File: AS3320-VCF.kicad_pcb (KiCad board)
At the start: 2 copper layers, 71.2 x 131.1 mm, 48 parts, among them J1 SIGNAL_INPUT, J2 RESONANCE_CTRL_INPUT, J3 FREQ_CTRL_INPUT, J4 SIGNAL_OUTPUT, J5 -----, U1 AS3320

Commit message: Refactor
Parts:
- removed TP1: RES_CTRL, Seattle_Synths:TestPoint_Pad_4.0x4.0mm
- removed TP2: +12V, Seattle_Synths:TestPoint_Pad_4.0x4.0mm
- removed TP3: -12V, Seattle_Synths:TestPoint_Pad_4.0x4.0mm
- removed TP4: GND, Seattle_Synths:TestPoint_Pad_4.0x4.0mm
- removed TP5: FREQ_CTRL, Seattle_Synths:TestPoint_Pad_4.0x4.0mm
- removed TP6: INPUT, Seattle_Synths:TestPoint_Pad_4.0x4.0mm
- removed TP7: OUTPUT, Seattle_Synths:TestPoint_Pad_4.0x4.0mm
- added C10: 100nF, Seattle_Synths:C_0603_1608Metric, F.Cu at (147.8, 76.5)
- added C11: 470nF, Seattle_Synths:C_0603_1608Metric, F.Cu at (147.8, 83.2)
- added C12: 220pF, Seattle_Synths:C_0603_1608Metric, F.Cu at (92.2, 30.0)
- added C8: 470nF, Seattle_Synths:C_0603_1608Metric, F.Cu at (141.8, 83.2)
- added C9: 22pF, Seattle_Synths:C_0603_1608Metric, F.Cu at (140.2, 46.5)
- added J6: CV2_INPUT, Seattle_Synths:Jack_3.5mm_QingPu_WQP-PJ398SM_Vertical_CircularHoles, F.Cu at (18.8, 78.0)
- added J7: EURO_PWR_2x5, Seattle_Synths:3M_2510-6002UB, F.Cu at (117.0, 87.8)
- added J8: AUDIO_OUTPUT, Seattle_Synths:Jack_3.5mm_QingPu_WQP-PJ398SM_Vertical_CircularHoles, F.Cu at (158.2, 34.5)
- added R22: 91K, Seattle_Synths:R_0603_1608Metric, F.Cu at (84.8, 48.8)
- added R23: 91K, Seattle_Synths:R_0603_1608Metric, F.Cu at (84.8, 51.8)
- added R24: 100K, Seattle_Synths:R_0603_1608Metric, F.Cu at (84.8, 54.8)
- added R25: 240K, Seattle_Synths:R_0603_1608Metric, F.Cu at (84.8, 57.8)
- added R26: 240K, Seattle_Synths:R_0603_1608Metric, F.Cu at (84.8, 60.8)
- added R27: 51K, Seattle_Synths:R_0603_1608Metric, F.Cu at (93.8, 55.5)
- added R28: 1K, Seattle_Synths:R_0603_1608Metric, F.Cu at (105.0, 69.0)
- added R29: 1K, Seattle_Synths:R_0603_1608Metric, F.Cu at (124.5, 20.2)
- added R30: 100K, Seattle_Synths:R_0603_1608Metric, F.Cu at (128.2, 36.0)
- added R31: 180K, Seattle_Synths:R_0603_1608Metric, F.Cu at (130.5, 40.5)
- added R32: 300K, Seattle_Synths:R_0603_1608Metric, F.Cu at (140.2, 40.5)
- added R33: 1K, Seattle_Synths:R_0603_1608Metric, F.Cu at (149.2, 34.5)
- added RV3: 100K lin, Seattle_Synths:Potentiometer_Alpha_RD901F-40-00D_Single_Vertical, F.Cu at (29.2, 94.5)
- added RV4: 100K lin, Seattle_Synths:Potentiometer_Alpha_RD901F-40-00D_Single_Vertical, F.Cu at (29.2, 107.2)
- added RV5: 100K, Seattle_Synths:Potentiometer_Alpha_RD901F-40-00D_Single_Vertical, F.Cu at (36.0, 30.8)
- added RV6: 100K, Seattle_Synths:Potentiometer_Alpha_RD901F-40-00D_Single_Vertical, F.Cu at (36.0, 39.8)
- added RV7: 20K, Seattle_Synths:TRIM_3266W-1-102LF, F.Cu at (48.8, 64.5)
- added RV8: 1K5, Seattle_Synths:TRIM_3266W-1-102LF, F.Cu at (105.0, 63.0)
- added RV9: 100K, Seattle_Synths:TRIM_3266W-1-102LF, F.Cu at (130.5, 46.5)
- added U2: AS3320, Seattle_Synths:DIP-18_W7.62mm_Socket, F.Cu at (105.0, 47.2)
- added U3: TL082, Seattle_Synths:DIP-8_W7.62mm_Socket, F.Cu at (139.5, 34.5)
- C1: value 300pF -> 22pF; footprint Seattle_Synths:C_Disc_D7.5mm_W2.5mm_P5.00mm -> Seattle_Synths:C_0603_1608Metric
- C2: value 300pF -> 1µF; footprint Seattle_Synths:C_Disc_D7.5mm_W2.5mm_P5.00mm -> Seattle_Synths:CP_Radial_D5.0mm_P2.50mm
- C3, C4: value 300pF -> 220pF; footprint Seattle_Synths:C_Disc_D7.5mm_W2.5mm_P5.00mm -> Seattle_Synths:C_0603_1608Metric
- C5: value 1µF -> 220pF; footprint Seattle_Synths:CP_Radial_D5.0mm_P2.50mm -> Seattle_Synths:C_0603_1608Metric
- C6: value 10uF -> 1µF
- C7: value 10uF -> 100nF; footprint Seattle_Synths:CP_Radial_D5.0mm_P2.50mm -> Seattle_Synths:C_0603_1608Metric
- D1: footprint Seattle_Synths:LED_D5.0mm -> Seattle_Synths:D_0603_1608Metric; moved to F.Cu
- J1: value SIGNAL_INPUT -> AUDIO3_INPUT; moved to F.Cu
- J2: value RESONANCE_CTRL_INPUT -> AUDIO2_INPUT; moved to F.Cu
- J3: value FREQ_CTRL_INPUT -> AUDIO1_INPUT; moved to F.Cu
- J4: value SIGNAL_OUTPUT -> RES_INPUT; moved to F.Cu
- J5: value ----- -> 1V/OCT_INPUT; footprint Seattle_Synths:PinHeader_2x05_P2.54mm_Vertical -> Seattle_Synths:Jack_3.5mm_QingPu_WQP-PJ398SM_Vertical_CircularHoles
- R1: value 330R -> 51K; footprint Seattle_Synths:R_Axial_DIN0207_L6.3mm_D2.5mm_P10.16mm_Horizontal -> Seattle_Synths:R_0603_1608Metric
- R10, R19: value 1K8 -> 100K; footprint Seattle_Synths:R_Axial_DIN0207_L6.3mm_D2.5mm_P10.16mm_Horizontal -> Seattle_Synths:R_0603_1608Metric
- R11, R9: footprint Seattle_Synths:R_Axial_DIN0207_L6.3mm_D2.5mm_P10.16mm_Horizontal -> Seattle_Synths:R_0603_1608Metric
- R12: value 100K -> 15K; footprint Seattle_Synths:R_Axial_DIN0207_L6.3mm_D2.5mm_P10.16mm_Horizontal -> Seattle_Synths:R_0603_1608Metric
- R13: value 91K -> 36K; footprint Seattle_Synths:R_Axial_DIN0207_L6.3mm_D2.5mm_P10.16mm_Horizontal -> Seattle_Synths:R_0603_1608Metric
- R14: value 100K -> 56K; footprint Seattle_Synths:R_Axial_DIN0207_L6.3mm_D2.5mm_P10.16mm_Horizontal -> Seattle_Synths:R_0603_1608Metric
- R15: value 91K -> 1K; footprint Seattle_Synths:R_Axial_DIN0207_L6.3mm_D2.5mm_P10.16mm_Horizontal -> Seattle_Synths:R_0603_1608Metric
- R16, R18: value 100K -> 91K; footprint Seattle_Synths:R_Axial_DIN0207_L6.3mm_D2.5mm_P10.16mm_Horizontal -> Seattle_Synths:R_0603_1608Metric
- R17: value 91K -> 100K; footprint Seattle_Synths:R_Axial_DIN0207_L6.3mm_D2.5mm_P10.16mm_Horizontal -> Seattle_Synths:R_0603_1608Metric
- R2: value 72K -> 100K; footprint Seattle_Synths:R_Axial_DIN0207_L6.3mm_D2.5mm_P10.16mm_Horizontal -> Seattle_Synths:R_0603_1608Metric
- R20: value 51K -> 240K; footprint Seattle_Synths:R_Axial_DIN0207_L6.3mm_D2.5mm_P10.16mm_Horizontal -> Seattle_Synths:R_0603_1608Metric
- R21: value 330R -> 100K; footprint Seattle_Synths:R_Axial_DIN0207_L6.3mm_D2.5mm_P10.16mm_Horizontal -> Seattle_Synths:R_0603_1608Metric
- R3: value 50K -> 180K; footprint Seattle_Synths:R_Axial_DIN0207_L6.3mm_D2.5mm_P10.16mm_Horizontal -> Seattle_Synths:R_0603_1608Metric
- R4, R5: value 220K -> 100K; footprint Seattle_Synths:R_Axial_DIN0207_L6.3mm_D2.5mm_P10.16mm_Horizontal -> Seattle_Synths:R_0603_1608Metric
- R6: value 220K -> 150K; footprint Seattle_Synths:R_Axial_DIN0207_L6.3mm_D2.5mm_P10.16mm_Horizontal -> Seattle_Synths:R_0603_1608Metric
- R7: value 50K -> 1M5; footprint Seattle_Synths:R_Axial_DIN0207_L6.3mm_D2.5mm_P10.16mm_Horizontal -> Seattle_Synths:R_0603_1608Metric
- R8: value 100K -> 300K; footprint Seattle_Synths:R_Axial_DIN0207_L6.3mm_D2.5mm_P10.16mm_Horizontal -> Seattle_Synths:R_0603_1608Metric
- RV1: moved to F.Cu
- RV2: value 100K -> 100K lin; moved to F.Cu
- U1: value AS3320 -> TL082; footprint Seattle_Synths:DIP-18_W7.62mm_Socket -> Seattle_Synths:DIP-8_W7.62mm_Socket
- moved C1 164.0 mm to (52.5, 18.8)
- moved J1 156.3 mm to (18.8, 18.8), turned to 0 degrees
- moved J5 147.5 mm to (18.8, 67.5), turned to 0 degrees
- moved J3 139.2 mm to (18.8, 36.8), turned to 0 degrees
- moved C3 131.9 mm to (89.2, 27.0)
- moved C2 130.7 mm to (71.2, 30.8)
- moved J2 127.2 mm to (18.8, 27.8), turned to 0 degrees
- moved J4 125.9 mm to (18.8, 48.8), turned to 0 degrees
- moved RV1 116.7 mm to (27.8, 51.0), turned to 0 degrees
- moved RV2 116.1 mm to (29.2, 80.2), turned to 0 degrees
- moved R11 116.1 mm to (42.8, 64.5)
- moved R12 113.4 mm to (48.0, 37.5)
- moved R13 113.3 mm to (52.5, 30.8)
- moved R8 110.9 mm to (42.0, 18.8)
- moved R21 110.0 mm to (84.8, 45.8)
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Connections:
- C1 pad 1: GND -> Net-(C1-Pad1)
- C2 pad 2: GND -> Net-(C1-Pad2)
- C3 pad 1: GND -> Net-(C3-Pad1)
- C3 pad 2: Net-(C3-Pad2) -> GND
- C4 pad 1: Net-(C4-Pad1) -> GND
- C4 pad 2: GND -> Net-(C4-Pad2)
- C5 pad 1: /OUT4 -> Net-(C5-Pad1)
- C5 pad 2: /SIGNAL_OUTPUT -> GND
- C6 pad 1: -12V -> /OUT4
- C6 pad 2: GND -> Net-(C6-Pad2)
- C7 pad 2: +12V -> -12V
- J1 pad T: /SIGNAL_INPUT -> Net-(J1-PadT)
- J2 pad T: /RESONANCE_CTRL_INPUT -> Net-(J2-PadT)
- J3 pad T: /FREQ_CTRL_INPUT -> Net-(J3-PadT)
- J4 pad T: /SIGNAL_OUTPUT -> Net-(J4-PadT)
- J4 pad TN: (no net) -> Net-(J4-PadTN)
- R1 pad 1: -12V -> Net-(J4-PadTN)
- R1 pad 2: Net-(R1-Pad2) -> +12V
- R10 pad 1: GND -> Net-(C1-Pad1)
- R11 pad 2: /SIGNAL_INPUT -> Net-(R11-Pad2)
- R12 pad 1: Net-(R11-Pad1) -> Net-(R12-Pad1)
- R12 pad 2: /OUT1 -> GND
- R13 pad 1: Net-(R13-Pad1) -> Net-(C1-Pad2)
- R13 pad 2: /OUT1 -> Net-(C1-Pad1)
- R14 pad 1: Net-(R13-Pad1) -> Net-(R14-Pad1)
- R14 pad 2: /OUT2 -> /VCFI
- R15 pad 1: Net-(R15-Pad1) -> /VCFI
- R15 pad 2: /OUT2 -> GND
- R16 pad 1: Net-(R15-Pad1) -> Net-(R16-Pad1)
- R16 pad 2: /OUT3 -> Net-(C2-Pad1)
- R17 pad 1: Net-(R17-Pad1) -> Net-(R16-Pad1)
- R17 pad 2: /OUT3 -> /OUT1
- R18 pad 1: Net-(R17-Pad1) -> Net-(R18-Pad1)
- R18 pad 2: /OUT4 -> /OUT1
- R19 pad 1: Net-(R19-Pad1) -> Net-(R18-Pad1)
- R19 pad 2: -12V -> /OUT2
- R2 pad 1: +12V -> Net-(R2-Pad1)
- R2 pad 2: Net-(R2-Pad2) -> /IRES
- R20 pad 1: /SIGNAL_OUTPUT -> Net-(R18-Pad1)
- R20 pad 2: /VRES -> -12V
- R21 pad 1: Net-(D1-Pad2) -> Net-(R21-Pad1)
- R21 pad 2: +12V -> /OUT3
- R3 pad 1: Net-(R3-Pad1) -> Net-(R11-Pad2)
- R4 pad 1: Net-(R13-Pad1) -> Net-(R11-Pad2)
- R4 pad 2: -12V -> Net-(J5-PadT)
- R5 pad 1: Net-(R15-Pad1) -> Net-(R11-Pad2)
- R5 pad 2: -12V -> Net-(R5-Pad2)
- R6 pad 1: Net-(R17-Pad1) -> Net-(R11-Pad2)
- R6 pad 2: -12V -> Net-(R6-Pad2)
- R7 pad 1: Net-(R7-Pad1) -> Net-(R11-Pad2)
- R7 pad 2: +12V -> Net-(R7-Pad2)
- R8 pad 1: Net-(R8-Pad1) -> Net-(C1-Pad1)
- R8 pad 2: /RESONANCE_CTRL_INPUT -> Net-(J1-PadT)
- R9 pad 1: Net-(R10-Pad2) -> Net-(C1-Pad1)
- R9 pad 2: /FREQ_CTRL_INPUT -> Net-(R9-Pad2)
- RV1 pad 1: Net-(R2-Pad2) -> Net-(J4-PadT)
- RV1 pad 2: /RESONANCE_CTRL_INPUT -> Net-(R2-Pad1)
- RV1 pad 3: Net-(R1-Pad2) -> GND
- RV2 pad 1: Net-(R3-Pad1) -> Net-(J6-PadT)
- RV2 pad 2: /FREQ_CTRL_INPUT -> Net-(R5-Pad2)
- RV2 pad 3: Net-(R7-Pad1) -> GND
- U1 pad 1: Net-(R11-Pad1) -> Net-(C1-Pad2)
- U1 pad 2: Net-(R13-Pad1) -> Net-(C1-Pad1)
- U1 pad 3: GND -> Net-(R12-Pad1)
- U1 pad 4: Net-(C1-Pad2) -> -12V
- U1 pad 5: Net-(C3-Pad2) -> GND
- U1 pad 6: /OUT2 -> Net-(R11-Pad2)
- U1 pad 7: /OUT1 -> Net-(R14-Pad1)
- U1 pad 8: /VRES -> +12V
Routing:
- net GND: track 280.1 -> 0.00 mm
- net +12V: track 234.3 -> 0.00 mm
- net -12V: track 231.8 -> 0.00 mm
- net Net-(D1-Pad2): track 130.4 -> 0.00 mm, vias 1 -> 0
- net /FREQ_CTRL_INPUT: track 128.9 -> 0.00 mm
- net Net-(R17-Pad1): track 127.1 -> 0.00 mm
- net Net-(R15-Pad1): track 109.3 -> 0.00 mm
- net /SIGNAL_INPUT: track 103.6 -> 0.00 mm
- net Net-(C1-Pad2): track 102.6 -> 0.00 mm
- net Net-(R10-Pad2): track 101.0 -> 0.00 mm
- net /OUT4: track 100.4 -> 0.00 mm
- net Net-(C4-Pad1): track 91.4 -> 0.00 mm
- net Net-(C3-Pad2): track 89.4 -> 0.00 mm
- net Net-(C2-Pad1): track 89.0 -> 0.00 mm
- net Net-(R8-Pad1): track 83.1 -> 0.00 mm
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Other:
- board text added: "Seattle Synths SS-VCF-1 Rev. 2, 2020-12-07 Designed by Nathaniel Houk Made with love <3"
- board text removed: "Seattle Synths SS-VCF-1 Rev. 1 [2020-11-08]"
- board text removed: "This machine kills fascists."

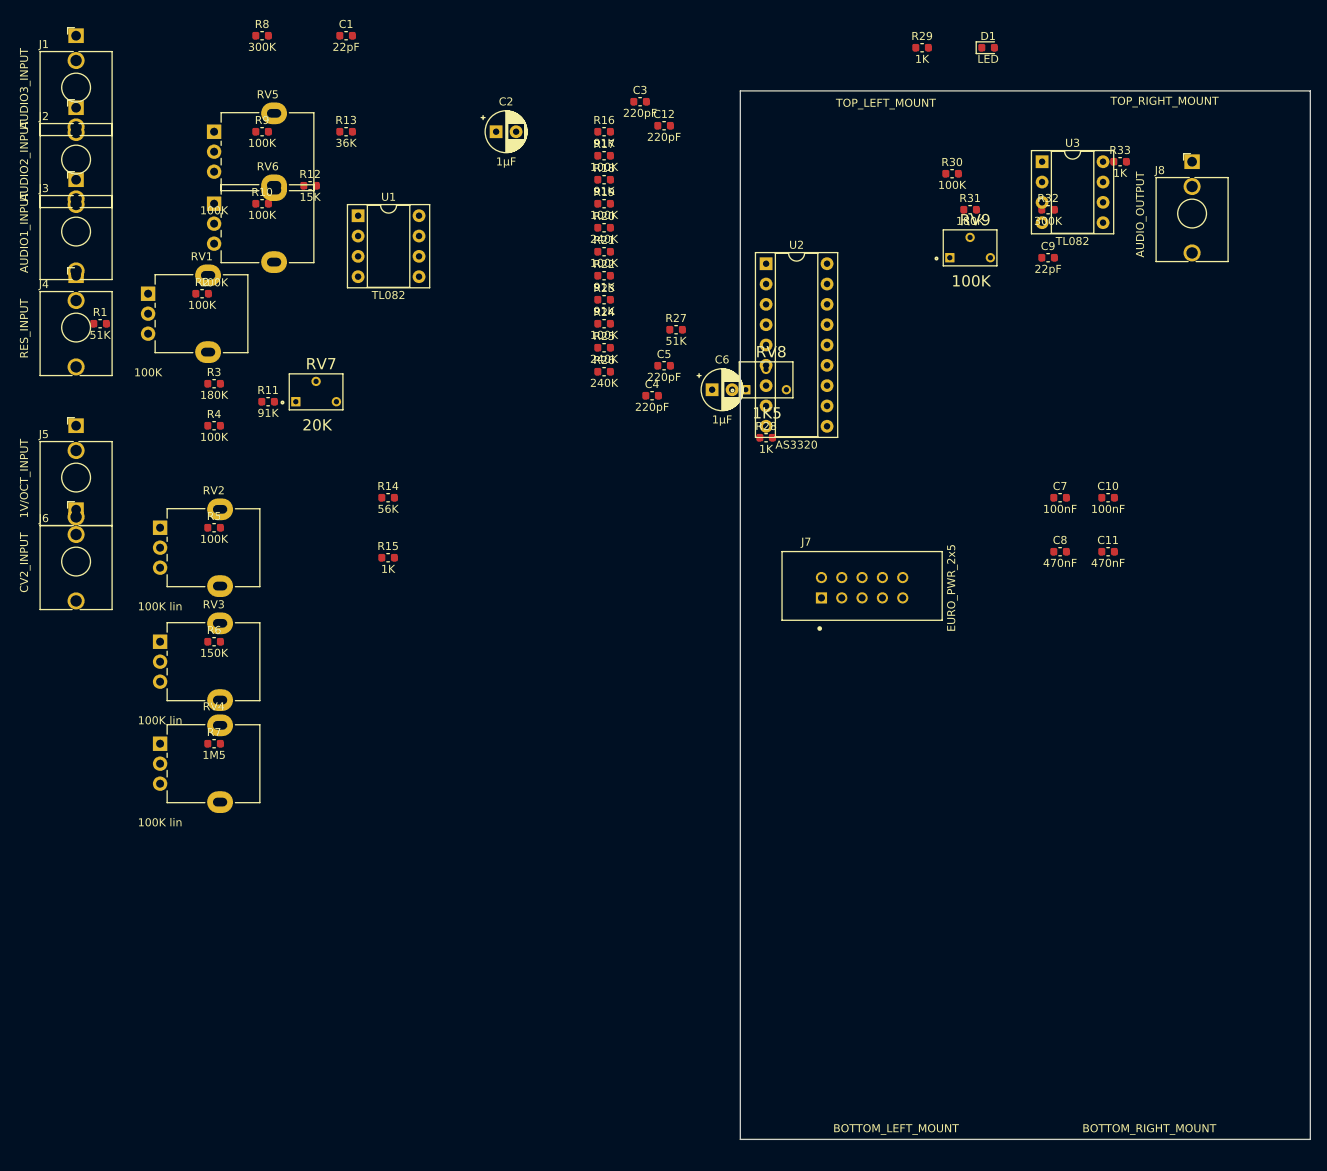
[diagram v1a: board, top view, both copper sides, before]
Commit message: Rev2. - Added ground plane, switched to SMD, new layout and rerouted.
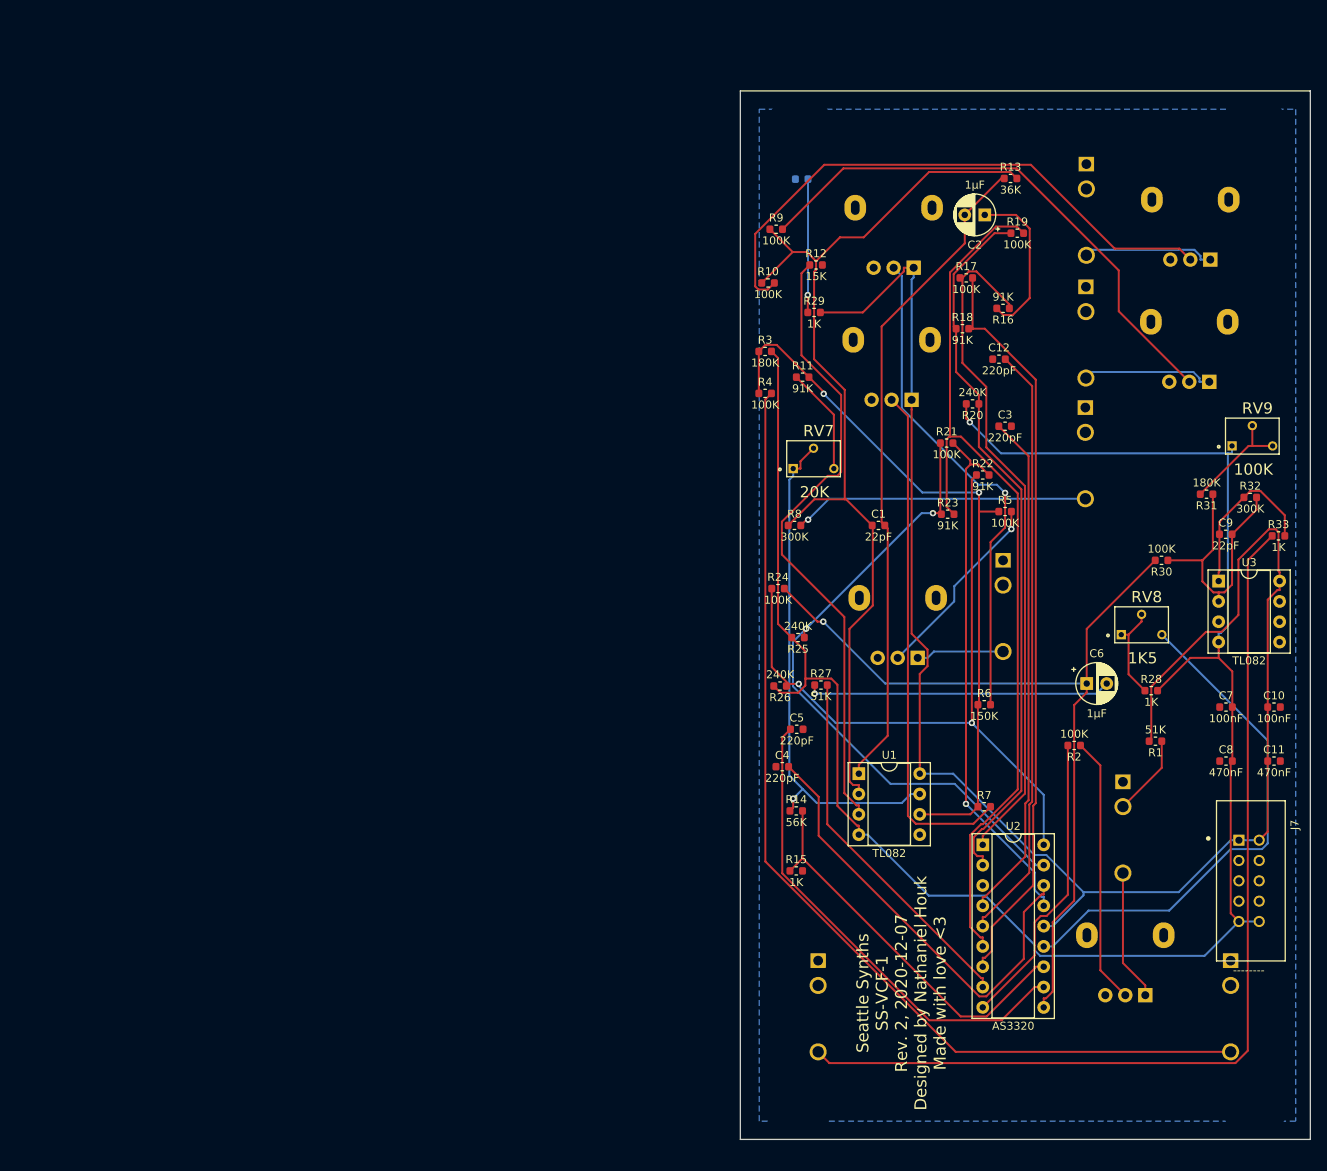
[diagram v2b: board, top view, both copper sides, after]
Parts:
- D1, J1, J2, J3, J4, J5, J6, J8, RV1, RV2, RV3, RV4, RV5, RV6: moved to B.Cu
- J7: value EURO_PWR_2x5 -> --------
- moved J5 159.1 mm to (163.1, 134.4), turned to 180 degrees
- moved RV1 152.4 mm to (152.4, 138.7), turned to 90 degrees
- moved J4 145.3 mm to (149.6, 112.0), turned to 180 degrees
- moved R1 141.9 mm to (153.7, 106.9), turned to 180 degrees
- moved J1 134.4 mm to (144.9, 65.2), turned to 180 degrees
- moved RV5 128.3 mm to (160.4, 62.0), turned to 90 degrees
- moved J2 128.2 mm to (145.0, 50.1), turned to 180 degrees
- moved J3 126.3 mm to (145.0, 34.8), turned to 180 degrees
- moved RV6 124.7 mm to (160.5, 46.7), turned to 90 degrees
- moved R2 122.8 mm to (143.5, 107.5), turned to 180 degrees
- moved J6 116.0 mm to (134.6, 84.3), turned to 180 degrees
- moved J8 110.3 mm to (111.5, 134.4), turned to 180 degrees
- moved RV3 105.2 mm to (123.4, 47.8), turned to 90 degrees
- moved RV4 103.3 mm to (123.2, 64.3), turned to 90 degrees
- moved R5 98.9 mm to (134.9, 78.2)
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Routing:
- net -12V: track 0.00 -> 238.5 mm, vias 0 -> 1
- net +12V: track 0.00 -> 212.0 mm
- net Net-(J5-PadT): track 0.00 -> 126.8 mm
- net Net-(C1-Pad1): track 0.00 -> 123.3 mm
- net Net-(J8-PadT): track 0.00 -> 120.5 mm
- net /OUT2: track 0.00 -> 114.2 mm
- net /OUT4: track 0.00 -> 104.5 mm, vias 0 -> 1
- net /OUT1: track 0.00 -> 93.7 mm
- net Net-(R11-Pad2): track 0.00 -> 90.4 mm, vias 0 -> 2
- net Net-(R18-Pad1): track 0.00 -> 90.1 mm
- net Net-(R22-Pad1): track 0.00 -> 88.4 mm, vias 0 -> 2
- net Net-(R16-Pad1): track 0.00 -> 85.0 mm
- net Net-(C1-Pad2): track 0.00 -> 82.8 mm
- net Net-(R21-Pad1): track 0.00 -> 81.5 mm, vias 0 -> 2
- net Net-(R12-Pad1): track 0.00 -> 79.1 mm
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- added copper zone on B.Cu, net GND

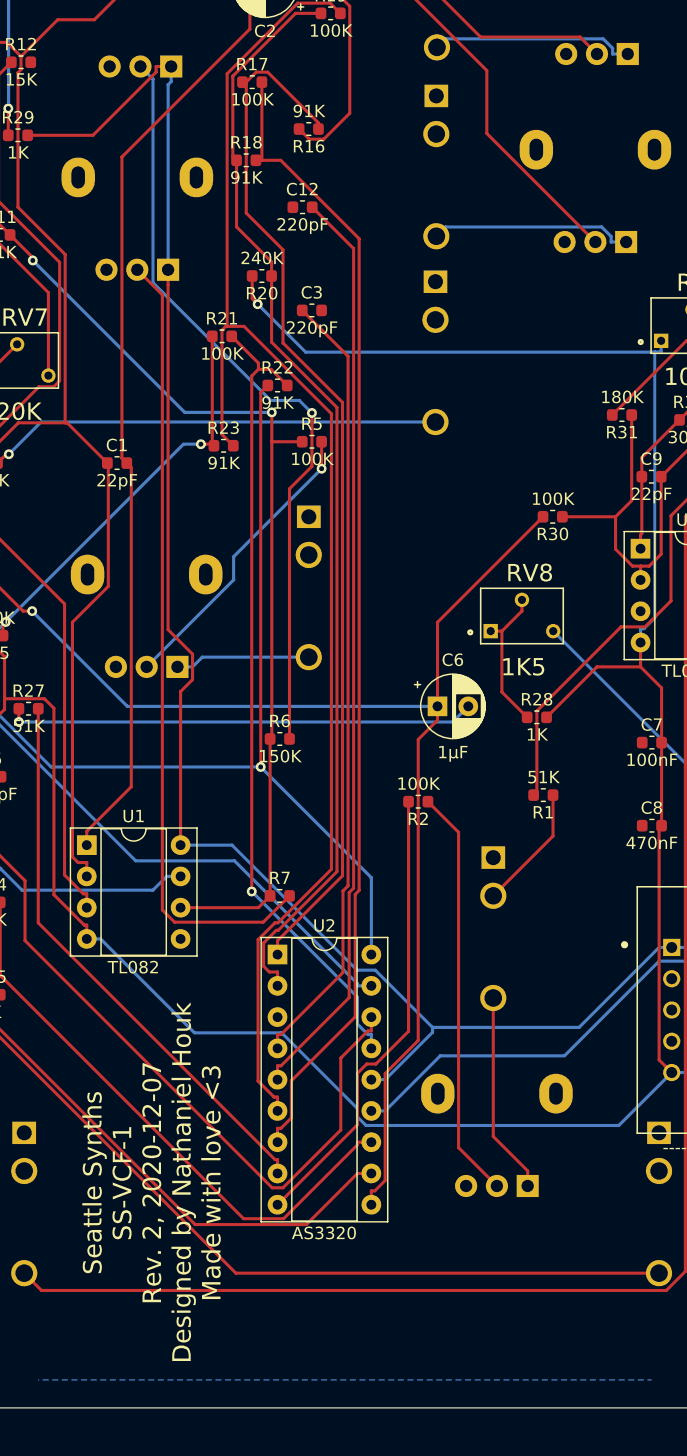
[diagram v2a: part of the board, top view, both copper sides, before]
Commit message: Rev. 2 - Update silk screen text.
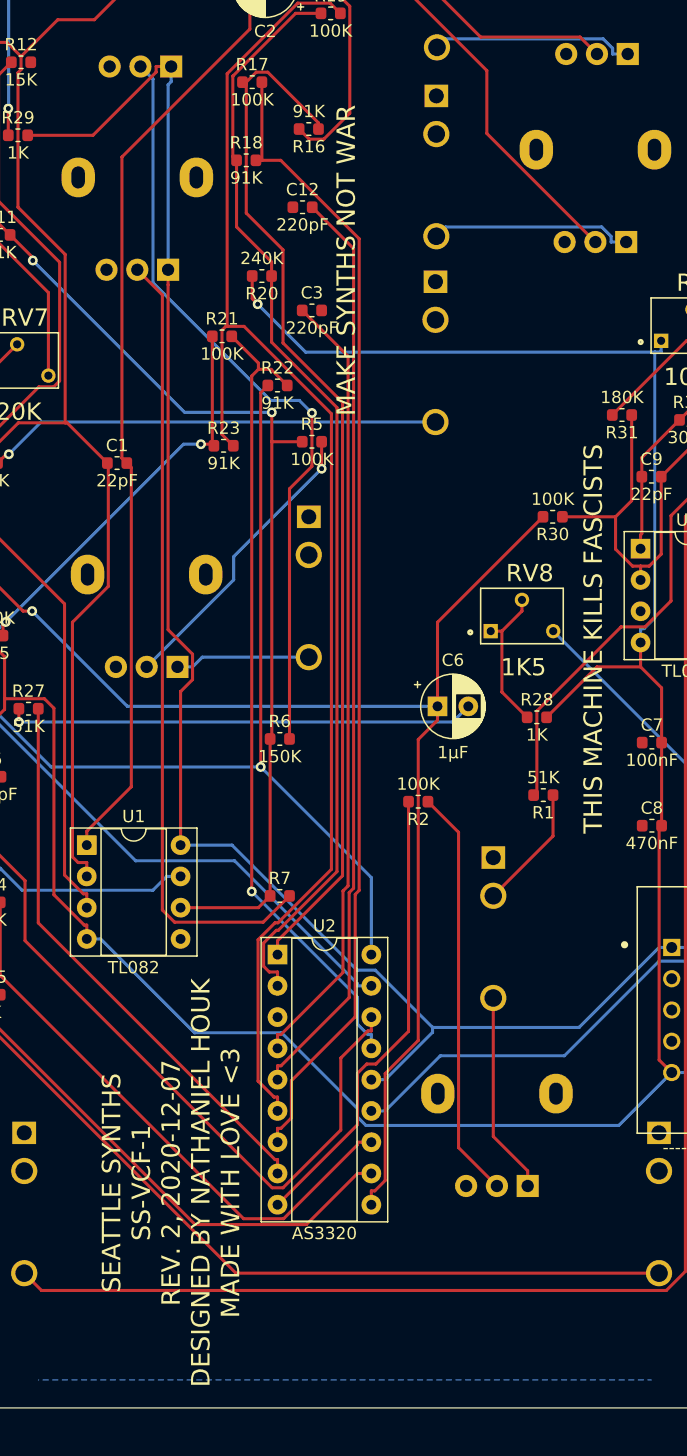
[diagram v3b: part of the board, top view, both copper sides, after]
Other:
- board text added: "MAKE SYNTHS NOT WAR"
- board text added: "SEATTLE SYNTHS SS-VCF-1 REV. 2, 2020-12-07 DESIGNED BY NATHANIEL HOUK MADE WITH LOVE <3"
- board text added: "THIS MACHINE KILLS FASCISTS"
- board text removed: "Seattle Synths SS-VCF-1 Rev. 2, 2020-12-07 Designed by Nathaniel Houk Made with love <3"
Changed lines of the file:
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@@
   (general
     (thickness 1.6)
-    (drawings 5)
+    (drawings 7)
     (tracks 454)
     (zones 0)
@@
     (pad "" np_thru_hole oval (at 0 0) (size 7.4 3.2) (drill oval 7.4 3.2) (layers *.Cu *.Mask))
   )
+  (gr_text "MAKE SYNTHS NOT WAR" (at 137.668 63.5 90) (layer F.SilkS)
+    (effects (font (size 1.5 1.5) (thickness 0.3)))
+  )
+  (gr_text "THIS MACHINE KILLS FASCISTS" (at 157.734 94.234 90) (layer F.SilkS)
+    (effects (font (size 1.5 1.5) (thickness 0.3)))
+  )
   (gr_line (start 173.03 25.65) (end 173.03 156.71) (layer Edge.Cuts) (width 0.05))
-  (gr_text "Seattle Synths\nSS-VCF-1\nRev. 2, 2020-12-07\nDesigned by Nathaniel Houk\nMade with love <3" (at 121.92 138.43 90) (layer F.SilkS)
+  (gr_text "SEATTLE SYNTHS\nSS-VCF-1\nREV. 2, 2020-12-07\nDESIGNED BY NATHANIEL HOUK\nMADE WITH LOVE <3" (at 123.444 138.43 90) (layer F.SilkS)
     (effects (font (size 1.5 1.5) (thickness 0.3)))
   )

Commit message: Refactor board
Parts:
- D1: value LED -> POWER
- J1: value AUDIO3_INPUT -> 3
- J2: value AUDIO2_INPUT -> 2
- J3: value AUDIO1_INPUT -> 1
- moved R24 62.5 mm to (154.4, 128.0)
- moved R19 61.1 mm to (127.5, 103.9)
- moved U1 52.7 mm to (162.1, 84.3)
- moved R16 51.1 mm to (137.7, 103.9)
- moved C12 49.7 mm to (137.7, 108.7)
- moved R27 49.4 mm to (143.8, 137.7)
- moved RV9 47.9 mm to (118.6, 78.5)
- moved R28 43.7 mm to (145.0, 143.5)
- moved C3 41.2 mm to (132.6, 108.7)
- moved R22 36.3 mm to (122.7, 108.7)
- moved R20 35.7 mm to (145.5, 97.3)
- moved R5 34.7 mm to (118.4, 108.7)
- moved C7 31.6 mm to (140.5, 80.0), turned to 180 degrees
- moved R14 30.8 mm to (109.0, 84.8)
- moved C6 30.3 mm to (145.8, 130.0), turned to 180 degrees
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- renumbered RV3 to FREQ, RV4 to RES
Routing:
- net GND: track 0.00 -> 421.0 mm
- net Net-(R28-Pad1): track 12.0 -> 97.0 mm, vias 0 -> 1
- net /VCFI: track 49.2 -> 115.2 mm
- net -12V: track 238.5 -> 192.8 mm, vias 1 -> 0
- net Net-(C2-Pad1): track 20.3 -> 64.1 mm
- net Net-(R11-Pad2): track 90.4 -> 133.3 mm
- net Net-(C12-Pad2): track 75.0 -> 34.2 mm
- net /OUT4: track 104.5 -> 68.7 mm, vias 1 -> 0
- net /OUT3: track 66.0 -> 101.2 mm, vias 1 -> 0
- net Net-(C3-Pad1): track 64.0 -> 31.9 mm
- net Net-(C1-Pad2): track 82.8 -> 114.2 mm
- net Net-(J1-PadT): track 37.0 -> 68.3 mm
- net Net-(C6-Pad2): track 38.1 -> 7.73 mm, vias 1 -> 0
- net +12V: track 212.0 -> 182.6 mm
- net Net-(R22-Pad1): track 88.4 -> 59.5 mm, vias 2 -> 1
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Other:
- board size 71.2 x 131.1 mm -> 71.2 x 128.5 mm
